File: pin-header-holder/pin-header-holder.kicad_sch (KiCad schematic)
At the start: 5 parts, among them J1 61302021821, J2 653004114822, J3 To BMS

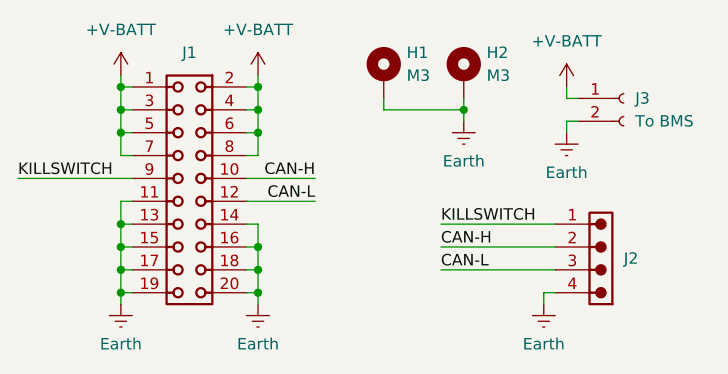
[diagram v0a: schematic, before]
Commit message: This shit needs rework for pogo pads
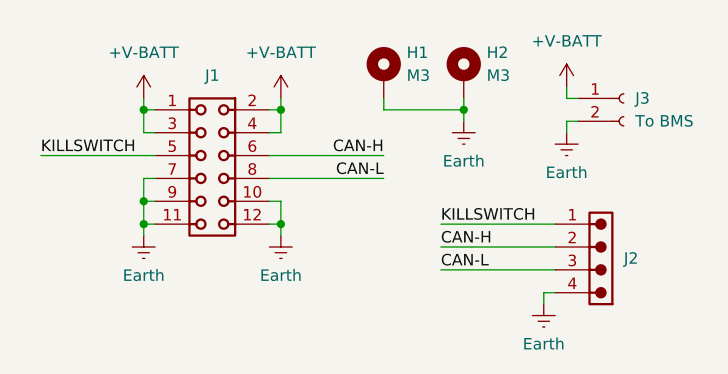
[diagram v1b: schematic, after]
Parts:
- removed J1: 61302021821, Connector_THT_Wurth:J_Wurth_WR-PHD_61302021821, symbol Connector_Wurth_WR-PHD:61302021821
- added J1: 61301221821, Connector_Harwin:Harwin_LTek-Male_2x06_P2.00mm_Vertical, symbol Connector_Wurth_WR-PHD:61301221821
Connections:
- net +V-BATT: now also J1.1, J1.2, J1.3, J1.4
- net CAN-H: now also J1.6
- net CAN-L: now also J1.8
- net Earth: now also J1.10, J1.11, J1.12, J1.7, J1.9
- net KILLSWITCH: now also J1.5
